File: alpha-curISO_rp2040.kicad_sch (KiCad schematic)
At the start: 20 parts, among them U1 RP2040

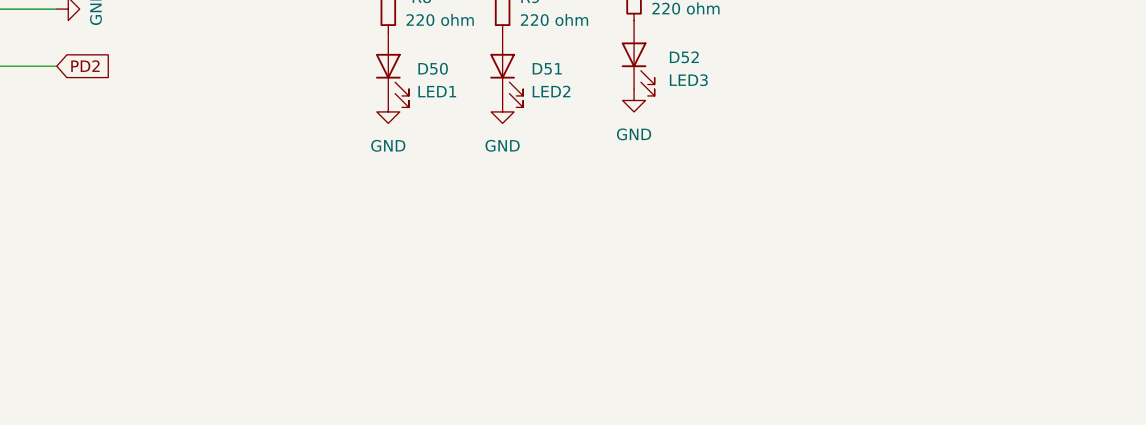
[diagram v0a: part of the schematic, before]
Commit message: MCU routing, RGB leds
MCU first routing draft finished

added RGB leds instead of diodes
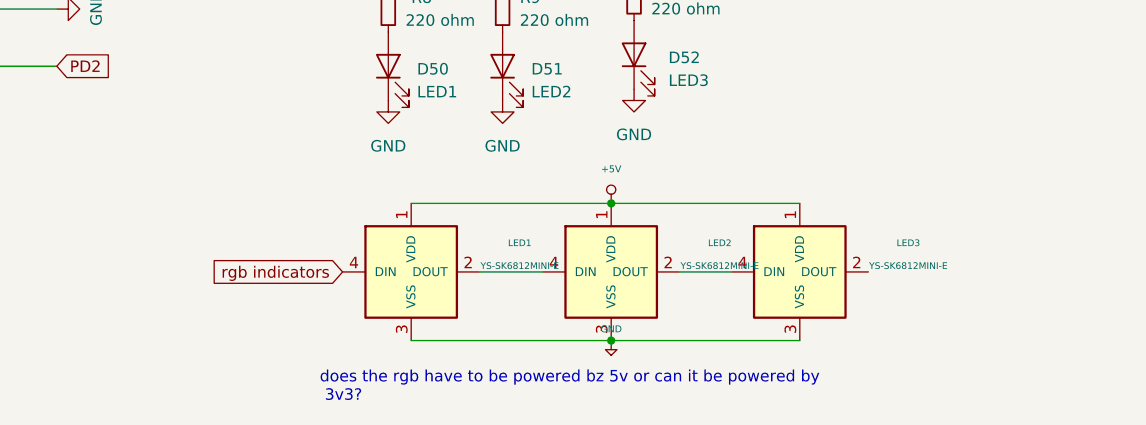
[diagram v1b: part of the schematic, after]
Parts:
- added LED1, LED2, LED3: YS-SK6812MINI-E, Keebio-Parts:SK6812-MINI-E, symbol kbd:YS-SK6812MINI-E
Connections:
- net +5V: now also LED1.1 (VDD), LED1.3 (VSS), LED2.1 (VDD), LED2.3 (VSS), LED3.1 (VDD), LED3.3 (VSS)
- new net: LED1.2 (DOUT), LED2.4 (DIN)
- new net: LED2.2 (DOUT), LED3.4 (DIN)
- new net rgb indicators: LED1.4 (DIN)
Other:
- note added: "does the rgb have to be powered bz 5v or can it be powered by 3v3?"
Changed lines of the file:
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@@
   (junction (at 102.235 222.25) (diameter 0) (color 0 0 0 0)
   )
+  (junction (at 195.58 231.14) (diameter 0) (color 0 0 0 0)
+  )
   (junction (at 102.235 209.55) (diameter 0) (color 0 0 0 0)
   )
@@
   (junction (at 52.07 29.21) (diameter 0) (color 0 0 0 0)
   )
+  (junction (at 195.58 246.38) (diameter 0) (color 0 0 0 0)
+  )
   (junction (at 126.365 195.58) (diameter 0) (color 0 0 0 0)
   )
@@
     (stroke (width 0) (type default) (color 0 0 0 0))
   )
+  (wire (pts (xy 180.975 238.76) (xy 187.96 238.76))
+    (stroke (width 0) (type default) (color 0 0 0 0))
+  )
   (wire (pts (xy 117.475 203.2) (xy 126.365 203.2))
     (stroke (width 0) (type default) (color 0 0 0 0))
@@
     (stroke (width 0) (type default) (color 0 0 0 0))
   )
+  (wire (pts (xy 195.58 246.38) (xy 216.535 246.38))
+    (stroke (width 0) (type default) (color 0 0 0 0))
+  )
   (wire (pts (xy 92.075 203.2) (xy 108.585 203.2))
     (stroke (width 0) (type default) (color 0 0 0 0))
   )
+  (wire (pts (xy 195.58 231.14) (xy 216.535 231.14))
+    (stroke (width 0) (type default) (color 0 0 0 0))
+  )
   (wire (pts (xy 34.29 36.83) (xy 39.37 36.83))
     (stroke (width 0) (type default) (color 0 0 0 0))
@@
     (stroke (width 0) (type default) (color 0 0 0 0))
   )
+  (wire (pts (xy 173.355 246.38) (xy 195.58 246.38))
+    (stroke (width 0) (type default) (color 0 0 0 0))
+  )
   (wire (pts (xy 29.21 48.26) (xy 31.496 48.26))
     (stroke (width 0) (type default) (color 0 0 0 0))
   )
+  (wire (pts (xy 173.355 231.14) (xy 195.58 231.14))
+    (stroke (width 0) (type default) (color 0 0 0 0))
+  )
   (wire (pts (xy 102.235 209.55) (xy 102.235 214.63))
     (stroke (width 0) (type default) (color 0 0 0 0))
@@
   )
   (wire (pts (xy 36.83 82.55) (xy 39.37 82.55))
+    (stroke (width 0) (type default) (color 0 0 0 0))
+  )
+  (wire (pts (xy 203.2 238.76) (xy 208.915 238.76))
     (stroke (width 0) (type default) (color 0 0 0 0))
   )
@@
   )
   (text "OLED" (at 57.785 189.865 0)
+    (effects (font (size 1.27 1.27)) (justify left bottom))
+  )
+  (text "does the rgb have to be powered bz 5v or can it be powered by\n 3v3?"
+    (at 163.195 253.365 0)
     (effects (font (size 1.27 1.27)) (justify left bottom))
   )
@@
     )
   )
+  (global_label "rgb indicators" (shape input) (at 165.735 238.76 180) (fields_autoplaced)
+    (effects (font (size 1.27 1.27)) (justify right))
+    (property "Intersheet References" "${INTERSHEET_REFS}" (id 0) (at 149.8357 238.6806 0)
+      (effects (font (size 1.27 1.27)) (justify right) hide)
+    )
+  )
   (global_label "SD2" (shape input) (at 39.37 109.22 180) (fields_autoplaced)
     (effects (font (size 1.27 1.27)) (justify right))
@@
     (pin "1")
   )
+  (symbol (lib_id "kbd:YS-SK6812MINI-E") (at 173.355 238.76 0) (unit 1)
+    (in_bom yes) (on_board yes) (fields_autoplaced)
+    (property "Reference" "LED1" (id 0) (at 185.42 235.5456 0)
+      (effects (font (size 0.7366 0.7366)))
+    )
+    (property "Value" "YS-SK6812MINI-E" (id 1) (at 185.42 238.0856 0)
+      (effects (font (size 0.7366 0.7366)))
+    )
+    (property "Footprint" "Keebio-Parts:SK6812-MINI-E" (id 2) (at 175.895 245.11 0)
+      (effects (font (size 1.27 1.27)) hide)
+    )
+    (property "Datasheet" "" (id 3) (at 175.895 245.11 0)
+      (effects (font (size 1.27 1.27)) hide)
+    )
+    (pin "1")
+    (pin "2")
+    (pin "3")
+    (pin "4")
+  )
   (symbol (lib_id "Device:R_Small") (at 34.29 34.29 0) (unit 1)
     (in_bom yes) (on_board yes) (fields_autoplaced)
@@
     )
     (pin "1")
+  )
+  (symbol (lib_id "kbd:YS-SK6812MINI-E") (at 195.58 238.76 0) (unit 1)
+    (in_bom yes) (on_board yes) (fields_autoplaced)
+    (property "Reference" "LED2" (id 0) (at 207.645 235.5456 0)
+      (effects (font (size 0.7366 0.7366)))
+    )
+    (property "Value" "YS-SK6812MINI-E" (id 1) (at 207.645 238.0856 0)
+      (effects (font (size 0.7366 0.7366)))
+    )
+    (property "Footprint" "Keebio-Parts:SK6812-MINI-E" (id 2) (at 198.12 245.11 0)
+      (effects (font (size 1.27 1.27)) hide)
+    )
+    (property "Datasheet" "" (id 3) (at 198.12 245.11 0)
+      (effects (font (size 1.27 1.27)) hide)
+    )
+    (pin "1")
+    (pin "2")
+    (pin "3")
+    (pin "4")
   )
   (symbol (lib_id "power:+3V3") (at 34.29 29.21 0) (unit 1)
@@
     (pin "1")
   )
+  (symbol (lib_id "keyboard_parts:+5V") (at 195.58 231.14 0) (unit 1)
+    (in_bom yes) (on_board yes) (fields_autoplaced)
+    (property "Reference" "#PWR0143" (id 0) (at 195.58 231.902 0)
+      (effects (font (size 0.508 0.508)) hide)
+    )
+    (property "Value" "+5V" (id 1) (at 195.58 227.33 0)
+      (effects (font (size 0.762 0.762)))
+    )
+    (property "Footprint" "" (id 2) (at 195.58 231.14 0)
+      (effects (font (size 1.524 1.524)))
+    )
+    (property "Datasheet" "" (id 3) (at 195.58 231.14 0)
+      (effects (font (size 1.524 1.524)))
+    )
+    (pin "1")
+  )
   (symbol (lib_id "power:+1V1") (at 62.23 29.21 0) (unit 1)
     (in_bom yes) (on_board yes) (fields_autoplaced)
@@
     (property "Datasheet" "" (id 3) (at 39.37 119.38 0)
       (effects (font (size 1.27 1.27)) hide)
+    )
+    (pin "1")
+  )
+  (symbol (lib_id "keyboard_parts:GND") (at 195.58 246.38 0) (unit 1)
+    (in_bom yes) (on_board yes) (fields_autoplaced)
+    (property "Reference" "#PWR0144" (id 0) (at 195.58 245.11 0)
+      (effects (font (size 0.508 0.508)) hide)
+    )
+    (property "Value" "GND" (id 1) (at 195.58 245.11 0)
+      (effects (font (size 0.762 0.762)))
+    )
+    (property "Footprint" "" (id 2) (at 195.58 246.38 0)
+      (effects (font (size 1.524 1.524)))
+    )
+    (property "Datasheet" "" (id 3) (at 195.58 246.38 0)
+      (effects (font (size 1.524 1.524)))
     )
     (pin "1")
@@
     (pin "2")
   )
+  (symbol (lib_id "kbd:YS-SK6812MINI-E") (at 216.535 238.76 0) (unit 1)
+    (in_bom yes) (on_board yes) (fields_autoplaced)
+    (property "Reference" "LED3" (id 0) (at 228.6 235.5456 0)
+      (effects (font (size 0.7366 0.7366)))
+    )
+    (property "Value" "YS-SK6812MINI-E" (id 1) (at 228.6 238.0856 0)
+      (effects (font (size 0.7366 0.7366)))
+    )
+    (property "Footprint" "Keebio-Parts:SK6812-MINI-E" (id 2) (at 219.075 245.11 0)
+      (effects (font (size 1.27 1.27)) hide)
+    )
+    (property "Datasheet" "" (id 3) (at 219.075 245.11 0)
+      (effects (font (size 1.27 1.27)) hide)
+    )
+    (pin "1")
+    (pin "2")
+    (pin "3")
+    (pin "4")
+  )
   (symbol (lib_id "kbd:OLED") (at 61.595 208.915 90) (unit 1)
     (in_bom yes) (on_board yes) (fields_autoplaced)
@@
       (reference "#PWR0142") (unit 1) (value "GND") (footprint "")
     )
+    (path "/57addf5b-74f0-433c-ac5f-3fa9f09d4d6d"
+      (reference "#PWR0143") (unit 1) (value "+5V") (footprint "")
+    )
+    (path "/8c46b104-0ada-4217-82ad-3db9df378af3"
+      (reference "#PWR0144") (unit 1) (value "GND") (footprint "")
+    )
     (path "/ed815977-8ce9-43bf-9f7d-c601496617ea/cce79384-81e6-4921-84d5-1511ce8fbc31"
       (reference "C1") (unit 1) (value "22pF") (footprint "Capacitor_SMD:C_0402_1005Metric")
@@
       (reference "J2") (unit 1) (value "USB_C_Receptacle_USB2.0") (footprint "Connector_USB:USB_C_Receptacle_HRO_TYPE-C-31-M-12")
     )
+    (path "/1e9baeb4-f548-45b2-aad9-c2fd14e7bd11"
+      (reference "LED1") (unit 1) (value "YS-SK6812MINI-E") (footprint "Keebio-Parts:SK6812-MINI-E")
+    )
+    (path "/25d16801-c138-4963-93cd-7f5f4e1f6e49"
+      (reference "LED2") (unit 1) (value "YS-SK6812MINI-E") (footprint "Keebio-Parts:SK6812-MINI-E")
+    )
+    (path "/deebd5d7-b803-4153-ba7d-0ef95e2180a5"
+      (reference "LED3") (unit 1) (value "YS-SK6812MINI-E") (footprint "Keebio-Parts:SK6812-MINI-E")
+    )
     (path "/dfecb933-f3c0-434b-ac04-862b97ea046c"
       (reference "OL1") (unit 1) (value "OLED") (footprint "kbd:OLED_v2")
@@
     )
     (path "/74380d57-f0c1-489b-a62c-a123199ad76d/f7de924a-1f22-4383-87ed-af0a273947eb"
-      (reference "SW44(4)1") (unit 1) (value "SW_Push_45deg") (footprint "")
+      (reference "SW44(4)1") (unit 1) (value "SW_Push_45deg") (footprint "CherryMX_4.00u:CherryMX_4.00u")
     )
     (path "/74380d57-f0c1-489b-a62c-a123199ad76d/9b81f541-be3a-4977-9960-1d213c0abb40"

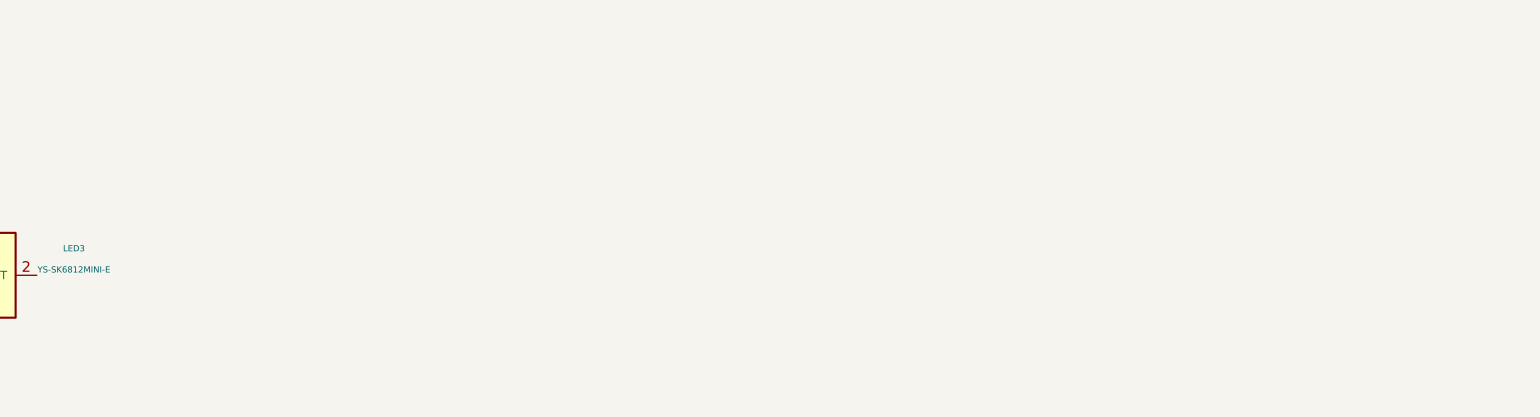
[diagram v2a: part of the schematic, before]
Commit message: added underglow to schematics
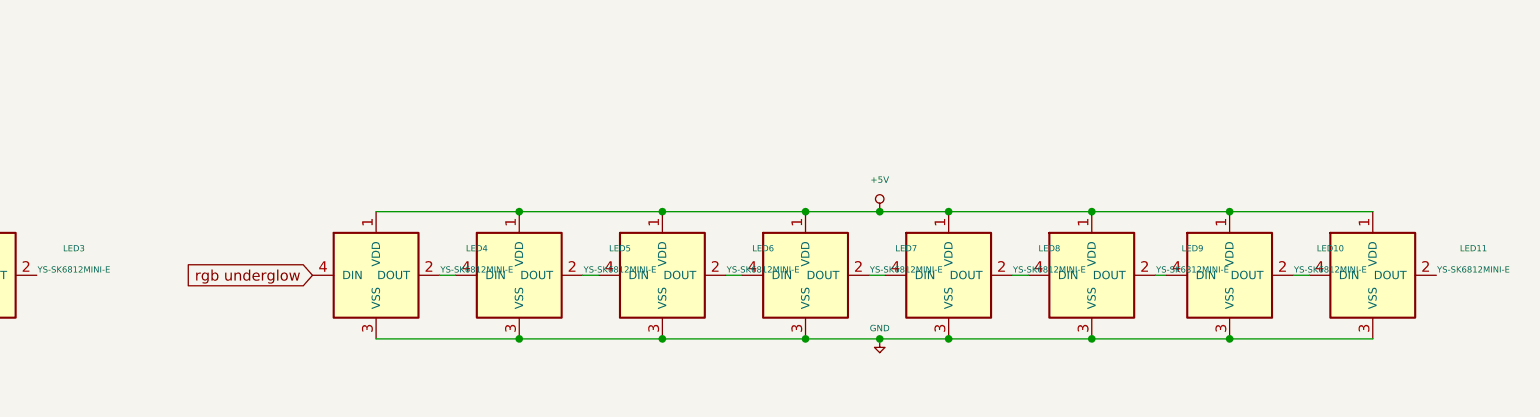
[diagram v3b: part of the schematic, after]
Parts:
- added LED10, LED11, LED4, LED5, LED6, LED7, LED8, LED9: YS-SK6812MINI-E, CrumpPrints:WS2812-2020, symbol kbd:YS-SK6812MINI-E
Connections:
- net +5V: now also LED10.1 (VDD), LED10.3 (VSS), LED11.1 (VDD), LED11.3 (VSS), LED4.1 (VDD), LED4.3 (VSS), LED5.1 (VDD), LED5.3 (VSS), LED6.1 (VDD), LED6.3 (VSS), LED7.1 (VDD), LED7.3 (VSS), LED8.1 (VDD), LED8.3 (VSS), LED9.1 (VDD), LED9.3 (VSS)
- new net: LED5.2 (DOUT), LED6.4 (DIN)
- new net: LED4.2 (DOUT), LED5.4 (DIN)
- new net: LED10.4 (DIN), LED9.2 (DOUT)
- new net: LED8.2 (DOUT), LED9.4 (DIN)
- new net: LED6.2 (DOUT), LED7.4 (DIN)
- new net: LED7.2 (DOUT), LED8.4 (DIN)
- new net: LED10.2 (DOUT), LED11.4 (DIN)
- new net rgb underglow: LED4.4 (DIN)

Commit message: galvy edits - start routing testing
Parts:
- removed TP1: TPGND, TestPoint:TestPoint_THTPad_1.0x1.0mm_Drill0.5mm, symbol Connector:TestPoint
- removed TP2: TPVCC, TestPoint:TestPoint_THTPad_1.0x1.0mm_Drill0.5mm, symbol Connector:TestPoint
- removed TP3: TPCLK, TestPoint:TestPoint_THTPad_1.0x1.0mm_Drill0.5mm, symbol Connector:TestPoint
- removed TP4: TPDATA, TestPoint:TestPoint_THTPad_1.0x1.0mm_Drill0.5mm, symbol Connector:TestPoint
- removed TP5: TPRST, TestPoint:TestPoint_THTPad_1.0x1.0mm_Drill0.5mm, symbol Connector:TestPoint
- added J2: SWD, Connector_PinSocket_2.54mm:PinSocket_1x05_P2.54mm_Vertical, symbol Connector_Generic:Conn_01x05
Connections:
- net +5V: now also J2.5 (Pin_5)
- net GND: now also J2.4 (Pin_4)
- net PD2: now also J2.1 (Pin_1)
- net PD5: now also J2.3 (Pin_3)
- net at C18.2, UR1.1: now also J2.2 (Pin_2)
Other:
- note added: "Trackpoint"
- note removed: "???"
- moved on the sheet: C18, OL1, UR1, UR2, UR3

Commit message: first bunch of routing
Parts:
- removed D50: LED1, Keebio-Parts:LED_3mm, symbol ComboDiode:LED
- removed D51: LED2, Keebio-Parts:LED_3mm, symbol ComboDiode:LED
- removed D52: LED3, Keebio-Parts:LED_3mm, symbol ComboDiode:LED
- removed R10, R8, R9: 220 ohm, Resistor_SMD:R_0402_1005Metric, symbol ComboDiode:R_Small
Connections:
- net +5V: no longer LED1.3 (VSS), LED10.3 (VSS), LED11.3 (VSS), LED2.3 (VSS), LED3.3 (VSS), LED4.3 (VSS), LED5.3 (VSS), LED6.3 (VSS), LED7.3 (VSS), LED8.3 (VSS), LED9.3 (VSS)
- net GND: now also LED1.3 (VSS), LED10.3 (VSS), LED11.3 (VSS), LED2.3 (VSS), LED3.3 (VSS), LED4.3 (VSS), LED5.3 (VSS), LED6.3 (VSS), LED7.3 (VSS), LED8.3 (VSS), LED9.3 (VSS)
- net PD2: now also U1.17 (GPIO14)
- net PD5: now also U1.18 (GPIO15)
- net COL4: now reaches U1.11 (GPIO8)
- net COL6: now reaches U1.12 (GPIO9)
- net COL5: now reaches U1.13 (GPIO10)
- net ROW0: now reaches U1.14 (GPIO11)
- net COL11: now reaches U1.15 (GPIO12)
- net COL12: now reaches U1.16 (GPIO13)
- net COL3: now reaches U1.2 (GPIO0)
- net COL2: now reaches U1.3 (GPIO1)
- net COL1: now reaches U1.4 (GPIO2)
- net COL0: now reaches U1.5 (GPIO3)
- net COL10: now reaches U1.6 (GPIO4)
- net COL9: now reaches U1.7 (GPIO5)
- net COL8: now reaches U1.8 (GPIO6)
- net COL7: now reaches U1.9 (GPIO7)

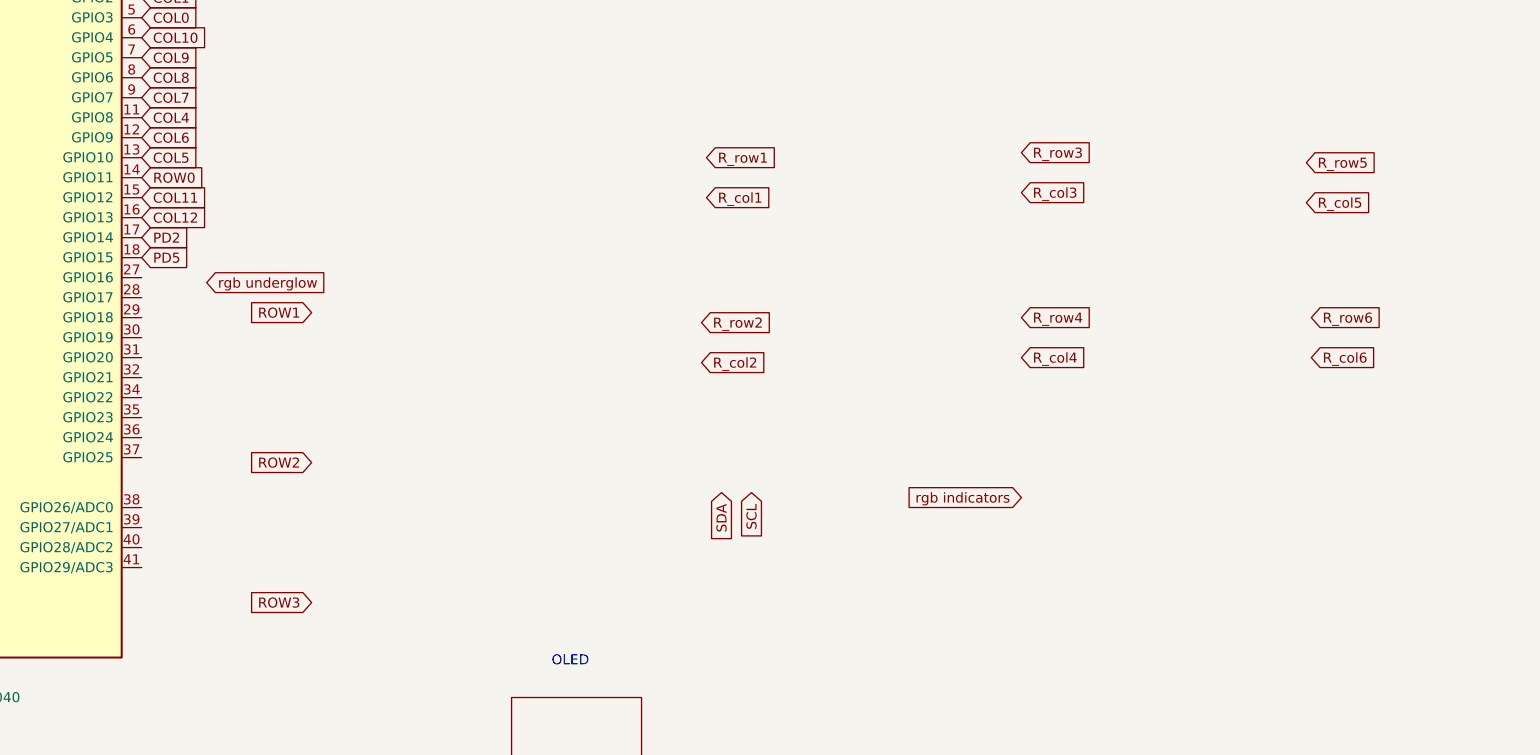
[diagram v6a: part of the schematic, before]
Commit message: finished first rough routing
short 1 pin
some GND are not connected to the GND layer
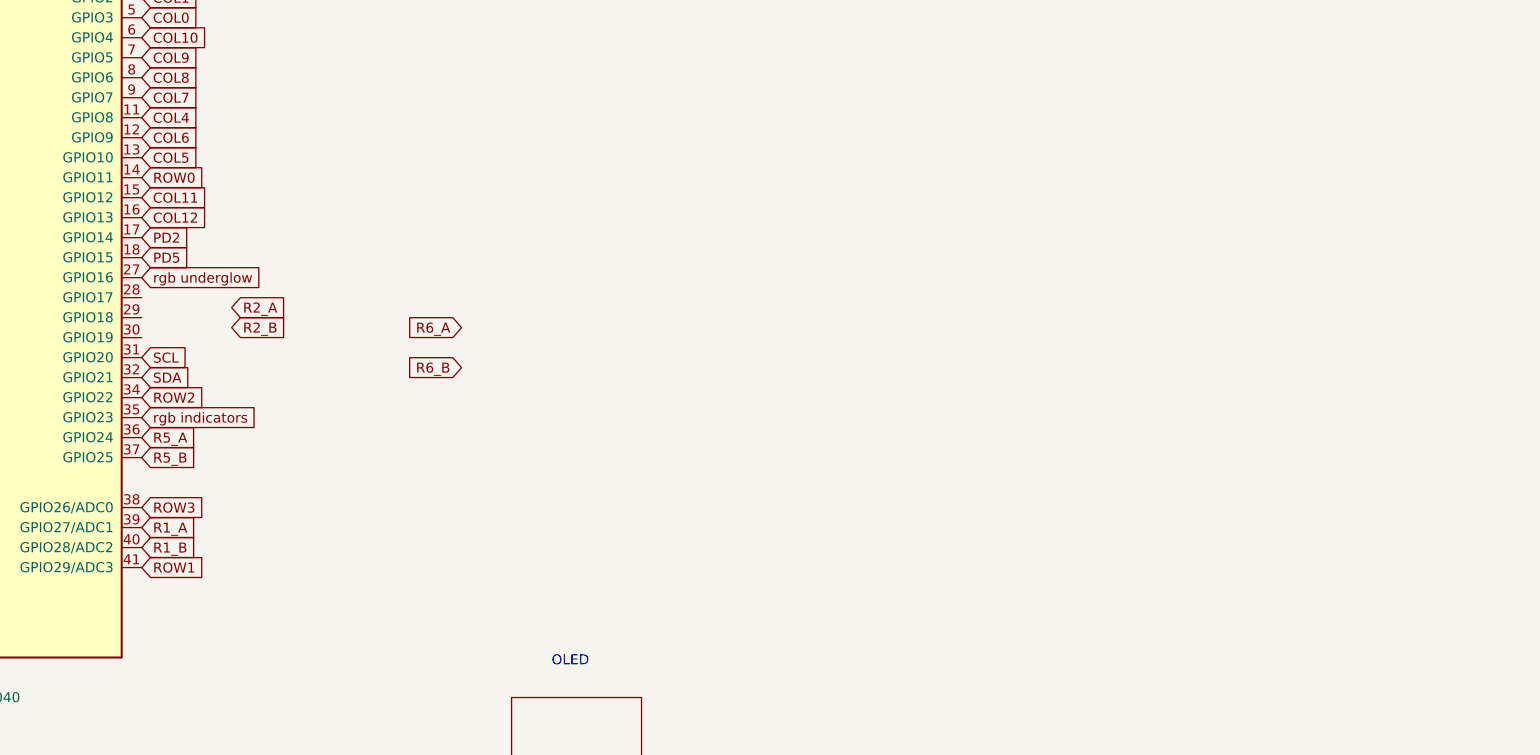
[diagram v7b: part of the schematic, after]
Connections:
- net ROW1: now also U1.41 (GPIO29/ADC3)
- net ROW2: now also U1.34 (GPIO22)
- net ROW3: now also U1.38 (GPIO26/ADC0)
- net SCL: now also U1.31 (GPIO20)
- net SDA: now also U1.32 (GPIO21)
- net rgb indicators: now also U1.35 (GPIO23)
- net rgb underglow: now also U1.27 (GPIO16)
- net R5_A: now reaches U1.36 (GPIO24)
- net R5_B: now reaches U1.37 (GPIO25)
- net R1_A: now reaches U1.39 (GPIO27/ADC1)
- net R1_B: now reaches U1.40 (GPIO28/ADC2)
